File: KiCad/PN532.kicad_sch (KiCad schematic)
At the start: 55 parts, among them J1 Bell, J2 SPOX, SW1 TAMPER, U1 PN532, U2 QR, U3 QR, Y1 27.12MHz

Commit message: Tidy up and new case
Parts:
- C1, C2: value 160pF 1% -> 160pF; footprint RevK:Cx2_0603 -> RevK:C_0603
- C11, C12, C14, C18, C7, C9: value 0.1uF -> 100nF
- C3, C4: value 22pF 1% -> 22pF
- C8: value 1nF 2% -> 1nF
- R1, R3: footprint RevK:Hidden -> RevK:R_0603_
- R2: footprint RevK:Hidden -> RevK:R_0805_
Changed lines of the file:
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@@
       (effects (font (size 1.27 1.27)) (justify left))
     )
-    (property "Value" "160pF 1%" (id 1) (at 58.42 95.25 0)
-      (effects (font (size 1.27 1.27)) (justify left))
-    )
-    (property "Footprint" "RevK:Cx2_0603" (id 2) (at 65.7352 101.6 0)
+    (property "Value" "160pF" (id 1) (at 58.42 95.25 0)
+      (effects (font (size 1.27 1.27)) (justify left))
+    )
+    (property "Footprint" "RevK:C_0603" (id 2) (at 65.7352 101.6 0)
       (effects (font (size 1.27 1.27)) hide)
     )
@@
     (in_bom yes) (on_board yes)
     (property "Reference" "C3" (id 0) (at 76.2 86.3092 90))
-    (property "Value" "22pF 1%" (id 1) (at 76.2 88.6206 90))
+    (property "Value" "22pF" (id 1) (at 76.2 88.6206 90))
     (property "Footprint" "RevK:C_0603" (id 2) (at 72.39 93.6752 0)
       (effects (font (size 1.27 1.27)) hide)
@@
     (in_bom yes) (on_board yes)
     (property "Reference" "C4" (id 0) (at 76.2 119.4308 90))
-    (property "Value" "22pF 1%" (id 1) (at 76.2 117.1194 90))
+    (property "Value" "22pF" (id 1) (at 76.2 117.1194 90))
     (property "Footprint" "RevK:C_0603" (id 2) (at 80.01 112.0648 0)
       (effects (font (size 1.27 1.27)) hide)
@@
     (in_bom yes) (on_board yes)
     (property "Reference" "C8" (id 0) (at 111.76 132.08 90))
-    (property "Value" "1nF 2%" (id 1) (at 111.76 122.9106 90))
+    (property "Value" "1nF" (id 1) (at 111.76 122.9106 90))
     (property "Footprint" "RevK:C_0603" (id 2) (at 107.95 127.9652 0)
       (effects (font (size 1.27 1.27)) hide)
@@
     (in_bom yes) (on_board yes)
     (property "Reference" "C9" (id 0) (at 118.11 111.7092 90))
-    (property "Value" "0.1uF" (id 1) (at 118.11 114.0206 90))
+    (property "Value" "100nF" (id 1) (at 118.11 114.0206 90))
     (property "Footprint" "RevK:C_0603" (id 2) (at 114.3 119.0752 0)
       (effects (font (size 1.27 1.27)) hide)
@@
       (effects (font (size 1.27 1.27)) (justify left))
     )
-    (property "Value" "0.1uF" (id 1) (at 101.6 82.55 0)
+    (property "Value" "100nF" (id 1) (at 101.6 82.55 0)
       (effects (font (size 1.27 1.27)) (justify left))
     )
@@
       (effects (font (size 1.27 1.27)) (justify left))
     )
-    (property "Value" "0.1uF" (id 1) (at 143.891 72.263 0)
+    (property "Value" "100nF" (id 1) (at 143.891 72.263 0)
       (effects (font (size 1.27 1.27)) (justify left))
     )
@@
       (effects (font (size 1.27 1.27)) (justify left))
     )
-    (property "Value" "0.1uF" (id 1) (at 113.03 55.88 0)
+    (property "Value" "100nF" (id 1) (at 113.03 55.88 0)
       (effects (font (size 1.27 1.27)) (justify left))
     )
@@
       (effects (font (size 1.27 1.27)) (justify left))
     )
-    (property "Value" "0.1uF" (id 1) (at 193.421 115.443 0)
+    (property "Value" "100nF" (id 1) (at 193.421 115.443 0)
       (effects (font (size 1.27 1.27)) (justify left))
     )
@@
       (effects (font (size 1.27 1.27)) (justify left))
     )
-    (property "Value" "0.1uF" (id 1) (at 127.381 143.383 0)
+    (property "Value" "100nF" (id 1) (at 127.381 143.383 0)
       (effects (font (size 1.27 1.27)) (justify left))
     )
@@
       (effects (font (size 1.27 1.27)) hide)
     )
+    (pin "1")
+    (pin "2")
+    (pin "6")
     (pin "3")
     (pin "4")
@@
       (effects (font (size 1.27 1.27)) hide)
     )
+    (pin "1")
+    (pin "2")
+    (pin "6")
     (pin "3")
     (pin "4")
@@
     (pin "2")
     (pin "6")
+    (pin "3")
+    (pin "4")
+    (pin "5")
   )
   (symbol (lib_id "Device:R") (at 233.68 152.4 270) (unit 1)
@@
     (pin "2")
     (pin "6")
+    (pin "3")
+    (pin "4")
+    (pin "5")
   )
   (symbol (lib_id "power:GND") (at 238.76 105.41 0) (mirror y) (unit 1)
@@
     (pin "2")
     (pin "6")
+    (pin "3")
+    (pin "4")
+    (pin "5")
   )
   (symbol (lib_id "Diode:BAV99S") (at 203.2 67.31 0) (mirror x) (unit 2)
@@
       (effects (font (size 1.27 1.27)) hide)
     )
+    (pin "1")
+    (pin "2")
+    (pin "6")
     (pin "3")
     (pin "4")
@@
       (effects (font (size 1.27 1.27)) (justify left))
     )
-    (property "Footprint" "RevK:Hidden" (id 2) (at 52.705 105.41 0)
+    (property "Footprint" "RevK:R_0603_" (id 2) (at 52.705 105.41 0)
       (effects (font (size 1.27 1.27)) hide)
     )
@@
       (effects (font (size 1.27 1.27)) (justify left))
     )
-    (property "Value" "160pF 1%" (id 1) (at 58.42 105.41 0)
-      (effects (font (size 1.27 1.27)) (justify left))
-    )
-    (property "Footprint" "RevK:Cx2_0603" (id 2) (at 65.7352 111.76 0)
+    (property "Value" "160pF" (id 1) (at 58.42 105.41 0)
+      (effects (font (size 1.27 1.27)) (justify left))
+    )
+    (property "Footprint" "RevK:C_0603" (id 2) (at 65.7352 111.76 0)
       (effects (font (size 1.27 1.27)) hide)
     )
@@
       (effects (font (size 1.27 1.27)) (justify left))
     )
-    (property "Footprint" "RevK:Hidden" (id 2) (at 52.705 100.33 0)
+    (property "Footprint" "RevK:R_0603_" (id 2) (at 52.705 100.33 0)
       (effects (font (size 1.27 1.27)) hide)
     )
@@
       (effects (font (size 1.27 1.27)) (justify left))
     )
-    (property "Footprint" "RevK:Hidden" (id 2) (at 52.705 102.87 0)
+    (property "Footprint" "RevK:R_0805_" (id 2) (at 52.705 102.87 0)
       (effects (font (size 1.27 1.27)) hide)
     )
@@
     )
     (path "/00000000-0000-0000-0000-000060756cae"
-      (reference "C1") (unit 1) (value "160pF 1%") (footprint "RevK:Cx2_0603")
+      (reference "C1") (unit 1) (value "160pF") (footprint "RevK:C_0603")
     )
     (path "/4b8d25e0-f830-4864-9f16-698fc7486e15"
-      (reference "C2") (unit 1) (value "160pF 1%") (footprint "RevK:Cx2_0603")
+      (reference "C2") (unit 1) (value "160pF") (footprint "RevK:C_0603")
     )
     (path "/00000000-0000-0000-0000-000060758ce7"
-      (reference "C3") (unit 1) (value "22pF 1%") (footprint "RevK:C_0603")
+      (reference "C3") (unit 1) (value "22pF") (footprint "RevK:C_0603")
     )
     (path "/00000000-0000-0000-0000-000060759861"
-      (reference "C4") (unit 1) (value "22pF 1%") (footprint "RevK:C_0603")
+      (reference "C4") (unit 1) (value "22pF") (footprint "RevK:C_0603")
     )
     (path "/00000000-0000-0000-0000-00006075a7aa"
@@
     )
     (path "/00000000-0000-0000-0000-00006075fd74"
-      (reference "C7") (unit 1) (value "0.1uF") (footprint "RevK:C_0603")
+      (reference "C7") (unit 1) (value "100nF") (footprint "RevK:C_0603")
     )
     (path "/00000000-0000-0000-0000-00006075c646"
-      (reference "C8") (unit 1) (value "1nF 2%") (footprint "RevK:C_0603")
+      (reference "C8") (unit 1) (value "1nF") (footprint "RevK:C_0603")
     )
     (path "/00000000-0000-0000-0000-00006075d8ac"
-      (reference "C9") (unit 1) (value "0.1uF") (footprint "RevK:C_0603")
+      (reference "C9") (unit 1) (value "100nF") (footprint "RevK:C_0603")
     )
     (path "/00000000-0000-0000-0000-00006075f2fd"
@@
     )
     (path "/00000000-0000-0000-0000-0000607617f2"
-      (reference "C11") (unit 1) (value "0.1uF") (footprint "RevK:C_0603")
+      (reference "C11") (unit 1) (value "100nF") (footprint "RevK:C_0603")
     )
     (path "/00000000-0000-0000-0000-00006078de67"
-      (reference "C12") (unit 1) (value "0.1uF") (footprint "RevK:C_0603")
+      (reference "C12") (unit 1) (value "100nF") (footprint "RevK:C_0603")
     )
     (path "/00000000-0000-0000-0000-000060761b18"
@@
     )
     (path "/00000000-0000-0000-0000-0000607608e5"
-      (reference "C14") (unit 1) (value "0.1uF") (footprint "RevK:C_0603")
+      (reference "C14") (unit 1) (value "100nF") (footprint "RevK:C_0603")
     )
     (path "/00000000-0000-0000-0000-000060993dc2"
@@
     )
     (path "/00000000-0000-0000-0000-0000607627aa"
-      (reference "C18") (unit 1) (value "0.1uF") (footprint "RevK:C_0603")
+      (reference "C18") (unit 1) (value "100nF") (footprint "RevK:C_0603")
     )
     (path "/00000000-0000-0000-0000-0000609f7a83"
@@
     )
     (path "/9d1ee0b7-8453-459c-a833-897b79b8b1c4"
-      (reference "R1") (unit 1) (value "0R") (footprint "RevK:Hidden")
+      (reference "R1") (unit 1) (value "0R") (footprint "RevK:R_0603_")
     )
     (path "/dc84d5ee-d81a-4f4d-a75f-84acaaa9d309"
-      (reference "R2") (unit 1) (value "0R") (footprint "RevK:Hidden")
+      (reference "R2") (unit 1) (value "0R") (footprint "RevK:R_0805_")
     )
     (path "/01990a6a-0667-4329-811a-e07a4a9e79e9"
-      (reference "R3") (unit 1) (value "0R") (footprint "RevK:Hidden")
+      (reference "R3") (unit 1) (value "0R") (footprint "RevK:R_0603_")
     )
     (path "/00000000-0000-0000-0000-00006075de03"

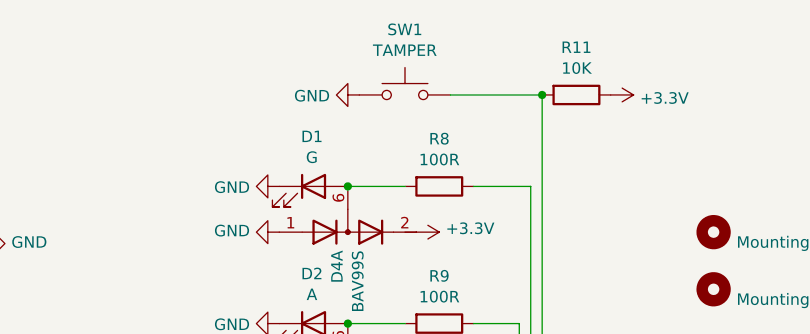
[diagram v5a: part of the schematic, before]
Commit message: Proper tamper switch
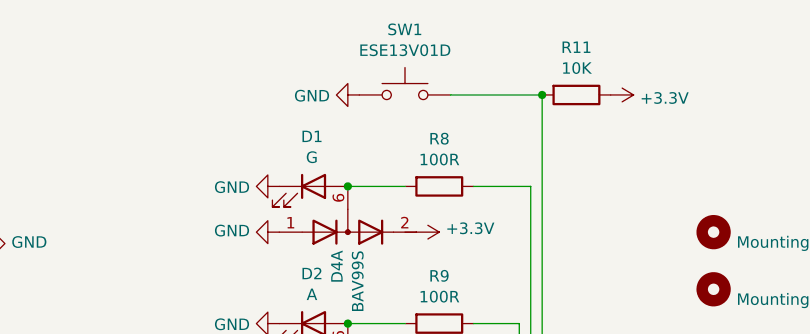
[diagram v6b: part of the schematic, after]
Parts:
- SW1: value TAMPER -> ESE13V01D; footprint RevK:SW_PUSH_6mm_SMD -> RevK:ESE13; Manufacturer E-Switch -> Panasonic; Part No LL3301NF065QG -> ESE13V01D; now in the parts list
- Y1: footprint RevK:Crystal-3.4x2.7 -> RevK:Crystal-3.2x2.5
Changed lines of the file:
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@@
       (effects (font (size 1.27 1.27)) (justify left))
     )
-    (property "Footprint" "RevK:Crystal-3.4x2.7" (id 2) (at 158.75 144.78 0)
+    (property "Footprint" "RevK:Crystal-3.2x2.5" (id 2) (at 158.75 144.78 0)
       (effects (font (size 1.27 1.27)) hide)
     )
@@
   )
   (symbol (lib_id "Switch:SW_Push") (at 209.55 20.32 0) (unit 1)
-    (in_bom no) (on_board yes)
+    (in_bom yes) (on_board yes)
     (property "Reference" "SW1" (id 0) (at 209.55 13.081 0))
-    (property "Value" "TAMPER" (id 1) (at 209.55 15.3924 0))
-    (property "Footprint" "RevK:SW_PUSH_6mm_SMD" (id 2) (at 209.55 15.24 0)
-      (effects (font (size 1.27 1.27)) hide)
-    )
-    (property "Datasheet" "https://www.mouser.co.uk/ProductDetail/612-LL3301NF065QG" (id 3) (at 209.55 15.24 0)
-      (effects (font (size 1.27 1.27)) hide)
-    )
-    (property "Part No" "LL3301NF065QG" (id 4) (at 209.55 20.32 0)
-      (effects (font (size 1.27 1.27)) hide)
-    )
-    (property "Manufacturer" "E-Switch" (id 5) (at 209.55 20.32 0)
+    (property "Value" "ESE13V01D" (id 1) (at 209.55 15.3924 0))
+    (property "Footprint" "RevK:ESE13" (id 2) (at 209.55 15.24 0)
+      (effects (font (size 1.27 1.27)) hide)
+    )
+    (property "Datasheet" "https://docs.rs-online.com/73f9/0900766b810acfc9.pdf" (id 3) (at 209.55 15.24 0)
+      (effects (font (size 1.27 1.27)) hide)
+    )
+    (property "Part No" "ESE13V01D" (id 4) (at 209.55 20.32 0)
+      (effects (font (size 1.27 1.27)) hide)
+    )
+    (property "Manufacturer" "Panasonic" (id 5) (at 209.55 20.32 0)
       (effects (font (size 1.27 1.27)) hide)
     )
@@
     )
     (path "/00000000-0000-0000-0000-00006076e91e"
-      (reference "SW1") (unit 1) (value "TAMPER") (footprint "RevK:SW_PUSH_6mm_SMD")
+      (reference "SW1") (unit 1) (value "ESE13V01D") (footprint "RevK:ESE13")
     )
     (path "/00000000-0000-0000-0000-0000609b72f2"
@@
     )
     (path "/00000000-0000-0000-0000-00006075caf9"
-      (reference "Y1") (unit 1) (value "27.12MHz") (footprint "RevK:Crystal-3.4x2.7")
-    )
-  )
+      (reference "Y1") (unit 1) (value "27.12MHz") (footprint "RevK:Crystal-3.2x2.5")
+    )
+  )
